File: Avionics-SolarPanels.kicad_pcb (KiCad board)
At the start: 4 copper layers, 82 x 100 mm, 208 parts, among them J1 200528-0100, J2 200528-0100, Q1 IRLML2803, Q17 NX3008NBKS, Q18 MBT2222ADW1T1, Q19 NX3008NBKS, Q2 SiRA99DP, Q20 MBT2222ADW1T1, Q21 NX3008NBKS, Q22 MBT2222ADW1T1, Q23 NX3008NBKS, Q24 MBT2222ADW1T1, Q25 NX3008NBKS, Q26 MBT2222ADW1T1, Q3 SiRA99DP, Q4 SiRA99DP, Q5 SiRA99DP, Q7 NX3008NBKS, Q8 MBT2222ADW1T1, U1 LTC4412xS6, U10 LTC3130, U11 LTC3130, U12 LTC3130, U13 ADM1176-1ARMZ-R7, U2 DRV8235RTER, U4 LTC4412xS6, U5 OPT4003DNPRQ1, U6 USBLC6-2P6, U8 LTC4412xS6

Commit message: v3.1 Updates
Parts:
- removed the C24 at (130.6, 116.6)
- removed the C25 at (130.6, 115.1)
- removed the C26 at (149.2, 89.2)
- removed the C36 at (149.9, 63.2)
- removed the F2 at (144.5, 94.2)
- removed the Q1 at (150.1, 93.5)
- removed the Q2 at (143.8, 89.2)
- removed R102, R103, R104, R105, R110, R111, R112, R113: 0R, Resistor_SMD:R_0603_1608Metric
- removed the R38 at (147.3, 93.5)
- removed the R39 at (147.6, 96.3)
- removed the R40 at (139.4, 94.5)
- removed the R41 at (137.7, 94.5)
- removed the R42 at (130.6, 113.5)
- removed the R43 at (132.3, 113.5)
- removed the R48 at (160.5, 90.4)
- removed the R50 at (162.1, 90.4)
- removed the U5 at (152.7, 63.2)
- removed the U6 at (133.6, 117.1)
- added ?: , clipboard:eb50a26b-5fb6-463a-8dd0-ee5887daaa13, F.Cu at (148.3, 55.0)
- added C1: 100n, Capacitor_SMD:C_0603_1608Metric, F.Cu at (148.2, 62.8)
- added C37: 10u, Capacitor_SMD:C_1210_3225Metric, B.Cu at (146.2, 91.0)
- added C43: 100n, Capacitor_SMD:C_0603_1608Metric, B.Cu at (129.5, 115.6)
- added F10: 500mA, Fuse:Fuse_0603_1608Metric, B.Cu at (141.5, 96.5)
- added Q16: SiRA99DP, Argus-Miscellaneous:PowerPAK SO-8, B.Cu at (140.0, 91.2)
- added Q17: IRLML2803, Package_TO_SOT_SMD:SOT-23, B.Cu at (135.1, 95.4)
- added R1: 0R, Resistor_SMD:R_0603_1608Metric, F.Cu at (149.7, 62.0)
- added R2: 0R, Resistor_SMD:R_0603_1608Metric, F.Cu at (149.7, 63.6)
- added R64: 2.7k, Resistor_SMD:R_0603_1608Metric, B.Cu at (132.7, 94.9)
- added R65: 10k, Resistor_SMD:R_0603_1608Metric, B.Cu at (131.9, 92.7)
- added R66: 4k7, Resistor_SMD:R_0603_1608Metric, B.Cu at (134.9, 92.7)
- added R67: 10k, Resistor_SMD:R_0603_1608Metric, B.Cu at (138.6, 96.5)
- added REF**: X Label, X Label, F.Cu at (152.4, 58.0)
- added Ref**: Val**, custom-footprints:ypanel, F.Cu at (169.4, 57.3)
- added U1: OPT4003DNPRQ1, Argus-IC:OPT4003, F.Cu at (152.4, 62.8)
- added U10: USBLC6-2SC6, Package_TO_SOT_SMD:SOT-23-6, B.Cu at (133.6, 114.4)
- added kibuzzard-680A9610: G***, kibuzzard-680A9610, B.Cu at (129.1, 94.8)
- C10: renamed from C7; value 1uF -> 1u
- C11: renamed from C8; value 22nF -> 22n
- C12: renamed from C9; value 22nF -> 22n
- C13: renamed from C11; value 1uF -> 1u
- C14: renamed from C12; value 47uF -> 47u
- C15: renamed from C10; value 4.7uF -> 4u7
- C16: renamed from C13; value 47uF -> 47u
- C17: renamed from C14; value 10uF -> 10u
- C18: renamed from C15; value 1uF -> 1u
- C19: renamed from C16; value 1uF -> 1u
- C2: renamed from C37; value 10nF -> 10n
- C20: renamed from C17; value 22nF -> 22n
- C21: renamed from C18; value 22nF -> 22n
- C22: renamed from C20; value 1uF -> 1u
- C23: renamed from C21; value 47uF -> 47u
- C24: renamed from C19; value 4.7uF -> 4u7
- C25: renamed from C23; value 47uF -> 47u
- C26: renamed from C39; value 10uF -> 10u
- C27: renamed from C40; value 1uF -> 1u
- C28: renamed from C41; value 1uF -> 1u
- C29: renamed from C42; value 22nF -> 22n
- C3: renamed from C38; value 10nF -> 10n
- C30: renamed from C43; value 22nF -> 22n
- C31: renamed from C45; value 1uF -> 1u
- C32: renamed from C46; value 47uF -> 47u
- C33: renamed from C44; value 4.7uF -> 4u7
- C34: renamed from C1; value 0.1uF -> 100n
- C35: renamed from C2; value 0.1uF -> 100n
- C36: renamed from C3; value 0.1uF -> 100n
- C38: renamed from C27; value 0.1uF -> 100n
- C39: renamed from C34; value 10nF -> 10n
- C4: renamed from C47; value 3.3nF -> 3n3
- C40: renamed from C35; value 10nF -> 10n
- C41: renamed from C22; value 1nF -> 1n
- C42: renamed from C28; value 0.1uF -> 100n
- C5: renamed from C48; value 10nF -> 10n
- C6: renamed from C49; value 10nF -> 10n
- C7: renamed from C4; value 47uF -> 47u
- C8: renamed from C5; value 10uF -> 10u
- C9: renamed from C6; value 1uF -> 1u
- F1: moved to B.Cu
- H1, H4: footprint MountingHole:MountingHole_3.2mm_M3_DIN965_Pad_TopBottom -> Argus-Miscellaneous:MountingHole_3.2mm_5.2mm_Slot_TopBottom
- H5, H6: footprint MountingHole:MountingHole_3mm_Pad_TopBottom -> MountingHole:MountingHole_2.2mm_M2_DIN965_Pad_TopOnly; moved to F.Cu
- J1, J2: value 200528-0100 -> 1-84952-0; footprint Argus-Connectors:Molex_200528-0100_1x10-1MP_P1.00mm_Horizontal -> Connector_FFC-FPC:TE_1-84952-0_1x10-1MP_P1.0mm_Horizontal
- L1, L2, L3: value 6.8uH -> 6.8u
- R10: renamed from R122; value 10K -> 10k
- R12: renamed from R119; value 100K -> 100k
- R13: renamed from R123; value 200K -> 200k
- R14: renamed from R120; value DNI (0R) -> 0R
- R19: renamed from R25; value 100K -> 100k
- R21: renamed from R35; value 200K -> 200k
- R26: value 100K -> 100k
- R28: renamed from R89; value 200K -> 200k
- R3: renamed from R115; value 10K -> 10k
- R33: renamed from R27; value 100K -> 100k
- R35: renamed from R109; value 200K -> 200k
- R36: value 2.7k -> 0R
- R37: value 10k -> 0R
- R38: renamed from R124; value ?R -> 0.01R
- R39: renamed from R125; value 1K -> 1k
- R4: renamed from R116; value 10K -> 10k
- R40: renamed from R129; value 10K -> 10k
- R41: renamed from R130; value 10K -> 10k
- R43: renamed from R127; value 100K -> 100k
- R44: renamed from R131; value 200K -> 200k
- R45: renamed from R128; value DNI (0R) -> 0R
- R46: renamed from R135; value 10K -> 10k
- R47: renamed from R136; value 10K -> 10k
- R49: renamed from R133; value 100K -> 100k
- R50: renamed from R137; value 200K -> 200k
- R51: renamed from R134; value DNI (0R) -> 0R
- R52: renamed from R1; value 0R (DNI) -> 0R
- R56: renamed from R5; value 0R (DNI) -> 0R
- R6: renamed from R107; value 100K -> 100k
- R60: renamed from R9; value 0R (DNI) -> 0R
- R7: renamed from R117; value 200K -> 200k
- R70: renamed from R86; value 10K -> 10k
- R71: renamed from R87; value 10K -> 10k
- R73: renamed from R85; value 100K -> 100k
- R74: renamed from R94; value 200K -> 200k
- R75: renamed from R95; value DNI (0R) -> 0R
- R76: renamed from R99; value 10K -> 10k
- R77: renamed from R100; value 10K -> 10k
- R79: renamed from R97; value 100K -> 100k
- R8: renamed from R114; value DNI (0R) -> 0R
- R80: renamed from R101; value 200K -> 200k
- R81: renamed from R98; value DNI (0R) -> 0R
- R9: renamed from R121; value 10K -> 10k
- SC1, SC2, SC4, SC5, SC6: value SM141K06L -> SM141K06TF
- moved F1 35.3 mm to (173.6, 84.8)
- moved C6 24.1 mm to (136.8, 73.1), turned to 90 degrees
- moved R40 23.8 mm to (131.1, 72.3), turned to 0 degrees
- moved R50 23.1 mm to (135.3, 73.1), turned to -90 degrees
- moved R49 22.4 mm to (133.6, 73.1), turned to -90 degrees
- moved R37 22.2 mm to (133.1, 109.9)
- moved R42 20.8 mm to (131.1, 73.8), turned to 0 degrees
- moved R36 20.2 mm to (129.7, 109.9), turned to 0 degrees
- moved Q8 18.1 mm to (135.9, 75.8), turned to 0 degrees
- moved Q5 16.5 mm to (131.3, 75.8), turned to 0 degrees
- moved R47 16.4 mm to (133.6, 76.0), turned to 90 degrees
- moved R51 14.4 mm to (135.9, 77.8), turned to 0 degrees
- moved R45 12.3 mm to (131.3, 77.8), turned to 180 degrees
- moved R9 12.2 mm to (168.7, 72.3), turned to 0 degrees
- moved C39 11.9 mm to (168.0, 99.4), turned to -90 degrees
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- renumbered F6 to F2, F7 to F3, F8 to F4, F9 to F5, F10 to F6, F3 to F7, F4 to F8, F5 to F9, Q20 to Q1, Q4 to Q10, Q5 to Q11, Q8 to Q12, Q7 to Q13, Q18 to Q14, Q17 to Q15, Q19 to Q2, Q22 to Q3, Q21 to Q4, Q24 to Q5, Q23 to Q6, Q26 to Q7, Q25 to Q8, Q3 to Q9, R118 to R11, R16 to R15, R17 to R16, R13 to R17, R22 to R18, R34 to R20, R18 to R22, R19 to R23, R14 to R24, R23 to R25, R88 to R27, R20 to R29, R21 to R30, R15 to R31, R24 to R32, R108 to R34, R126 to R42, R132 to R48, R106 to R5, R2 to R53, R3 to R54, R4 to R55, R6 to R57, R7 to R58, R8 to R59, R10 to R61, R11 to R62, R12 to R63, R33 to R68, R54 to R69, R60 to R72, R96 to R78, R28 to R82, R29 to R83, R30 to R84, R31 to R85, R49 to R86, R51 to R87, R32 to R88, R52 to R89, R53 to R90, U13 to U2, U1 to U3, U8 to U5, U10 to U6, U11 to U7, U12 to U8, U2 to U9
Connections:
- net /Coil Driver/A0_COIL renamed /Coil Driver/A0
- net /Coil Driver/A1_COIL renamed /Coil Driver/A1
- net /Solar Charger/I2C Single Protection4/DEVICE renamed /Solar Charger/I2C Single Protection2/DEVICE
- net /Solar Charger/I2C Single Protection5/DEVICE renamed /Solar Charger/I2C Single Protection3/DEVICE
- net /Solar Charger/MPPT1/VIN renamed /Solar Charger/DSOLAR1
- net /Solar Charger/MPPT2/VIN renamed /Solar Charger/DSOLAR2
- F1 pad 2: PERI_3V3 -> 3V3_P
- J2 pad 1: Net-(J2-Pin_1) -> /Interfaces/SCL_C
- J2 pad 2: Net-(J2-Pin_2) -> /Interfaces/SDA_C
- J2 pad 3: /Interfaces/COIL_DRIVER_EN_OR_MAIN_3V3 -> COIL_DRIVER_EN
- J2 pad 4: MAIN_3V3 -> 3V3_P
- J2 pad 5: /Interfaces/PERI_3V3_OR_GND -> 3V3_P
- R36 pad 1: COIL_DRIVER_EN -> GND
- R36 pad 2: Net-(D9-A) -> /Solar Charger/A0
- R37 pad 2: COIL_DRIVER_EN -> /Solar Charger/A1
- R40 pad 1: MAIN_3V3 -> 3V3_P
- R41 pad 1: MAIN_3V3 -> 3V3_P
- R43 pad 1: MAIN_3V3 -> 3V3_P
- R46 pad 1: MAIN_3V3 -> 3V3_P
- R47 pad 1: MAIN_3V3 -> 3V3_P
- R49 pad 1: MAIN_3V3 -> 3V3_P
- R68 pad 1: MAIN_3V3 -> 3V3_P
- R69 pad 2: PERI_3V3 -> 3V3_P
- R70 pad 1: MAIN_3V3 -> 3V3_P
- R71 pad 1: MAIN_3V3 -> 3V3_P
- R73 pad 1: MAIN_3V3 -> 3V3_P
- R76 pad 1: MAIN_3V3 -> 3V3_P
- R77 pad 1: MAIN_3V3 -> 3V3_P
- R79 pad 1: MAIN_3V3 -> 3V3_P
- R89 pad 1: MAIN_3V3 -> 3V3_P
- U2 pad 8: /Solar Charger/A0_S -> /Solar Charger/A0
- U2 pad 9: /Solar Charger/A1_S -> /Solar Charger/A1
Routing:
- net /Coil Driver/coil: track 18961.3 -> 14514.8 mm
- net PERI_3V3: track 101.5 -> 0.00 mm, vias 3 -> 0
- net GND: track 93.6 -> 0.00 mm, vias 172 -> 66
- net VBATT: track 57.2 -> 2.96 mm, vias 2 -> 6
- net MAIN_3V3: track 41.3 -> 0.00 mm, vias 12 -> 0
- net SCL: track 93.4 -> 131.4 mm, vias 3 -> 4
- net /Interfaces/COIL_DRIVER_EN_OR_MAIN_3V3: track 35.6 -> 0.00 mm, vias 2 -> 0
- net Net-(D1-K): track 54.4 -> 82.8 mm
- net /Light Sensor/LS_3V3: track 65.2 -> 37.3 mm, vias 4 -> 6
- net Net-(D4-K): track 55.2 -> 82.8 mm
- net Net-(D3-K): track 147.2 -> 174.5 mm
- net 3V3_P: track 0.00 -> 17.8 mm, vias 0 -> 16
- net /Light Sensor/ADDR_LS: track 17.4 -> 0.00 mm
- net /Solar Charger/I2C Single Protection3/DEVICE: track 26.0 -> 42.3 mm
- net COIL_DRIVER_EN: track 13.2 -> 27.5 mm, vias 0 -> 2
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- added copper zone on In2.Cu, net /Light Sensor/LS_3V3
- added copper zone on B.Cu, net 3V3_P
- added copper zone on In2.Cu, net 3V3_P
- added copper zone on B.Cu, net D_VSOLAR1
- added copper zone on B.Cu, net D_VSOLAR2
- added copper zone on B.Cu, net Net-(Q16-S)
- added copper zone on In2.Cu, net VBATT
- removed copper zone on In2.Cu, net MAIN_3V3
- removed copper zone on B.Cu, net Net-(Q2-S)
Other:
- outline, holes or cut-outs redrawn
- board text added: "ARGUS CUBESAT"
- board text added: "ARGUS Cubesat Carnegie Mellon University X/Y Solar Panel v3.1"
- board text added: "COIL DRIVER I2C BUS PROTECTION"
- board text added: "CURRENT SENSOR I2C BUS PROTECTION"
- board text added: "LIGHT SENSOR I2C BUS PROTECTION"
- board text added: "N"
- board text added: "P"
- board text added: "SENSE"
- board text added: "⊗"
- board text added: "⊙"
- board text removed: "ARGUS"
- board text removed: "ARGUS Cubesat Carnegie Mellon University X/Y Solar Panel v3"

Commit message: Local Stash
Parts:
- removed U10: USBLC6-2SC6, Package_TO_SOT_SMD:SOT-23-6
- added U11: D5V0P4UR6SO, Package_TO_SOT_SMD:SOT-23-6, B.Cu at (133.6, 114.4)
- R64: value 2.7k -> 2k7
- SC1, SC2, SC4, SC5, SC6: value SM141K06TF -> SM141K06TF/S; footprint Argus-Miscellaneous:SM141K06TF -> Argus-Miscellaneous:SM141K06TF_S
- SC3: value SM141K10TF -> SM141K10TF/S; footprint Argus-Miscellaneous:SM141K10TF -> Argus-Miscellaneous:SM141K10TF_S
- moved D1 0.51 mm to (114.6, 81.5)
- moved D4 0.51 mm to (190.2, 81.5)
- moved SC1 0.51 mm to (128.4, 81.5)
- moved SC4 0.51 mm to (176.4, 81.5)
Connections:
- J2 pad 1: /Interfaces/SCL_C -> SCL
- J2 pad 2: /Interfaces/SDA_C -> SDA
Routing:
- net Net-(D4-K): track 82.8 -> 75.5 mm
- net Net-(D1-K): track 82.8 -> 75.5 mm
- net SCL: track 131.4 -> 135.9 mm
- net SDA: track 135.1 -> 139.5 mm
- net Net-(D2-K): track 84.8 -> 81.8 mm
- net /Interfaces/SCL_C: track 2.95 -> 0.00 mm
- net /Interfaces/SDA_C: track 2.94 -> 0.00 mm
- net Net-(Q9-G): track 6.69 -> 6.03 mm
- net Net-(Q11-G): track 6.75 -> 6.10 mm
- net Net-(Q10-G): track 6.73 -> 6.15 mm
- net VBATT: track 2.96 -> 2.40 mm
- net /Solar Charger/VCHRG: track 2.96 -> 2.40 mm
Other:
- board text added: "3V3_P"
- board text removed: "M_3V3"
- board text removed: "P_3V3"

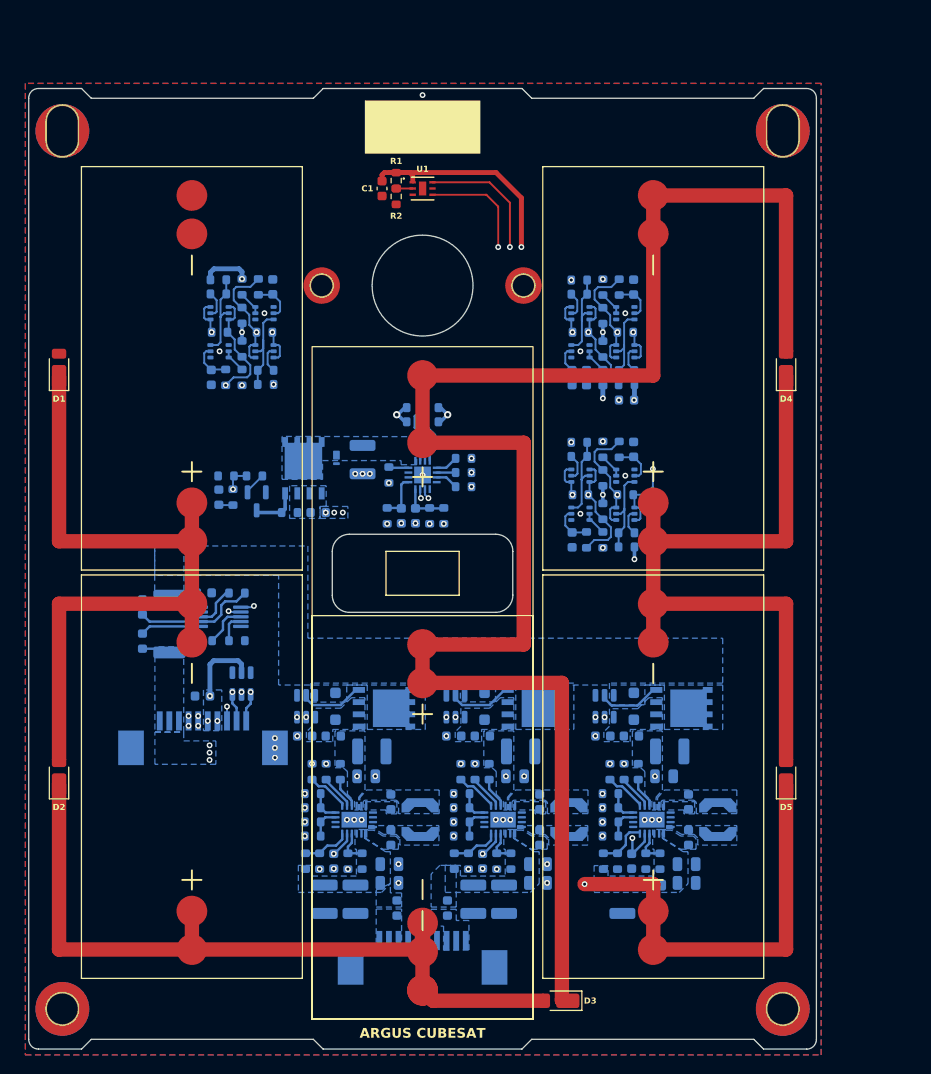
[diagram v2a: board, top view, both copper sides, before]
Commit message: Updated access port, added deployment sensor
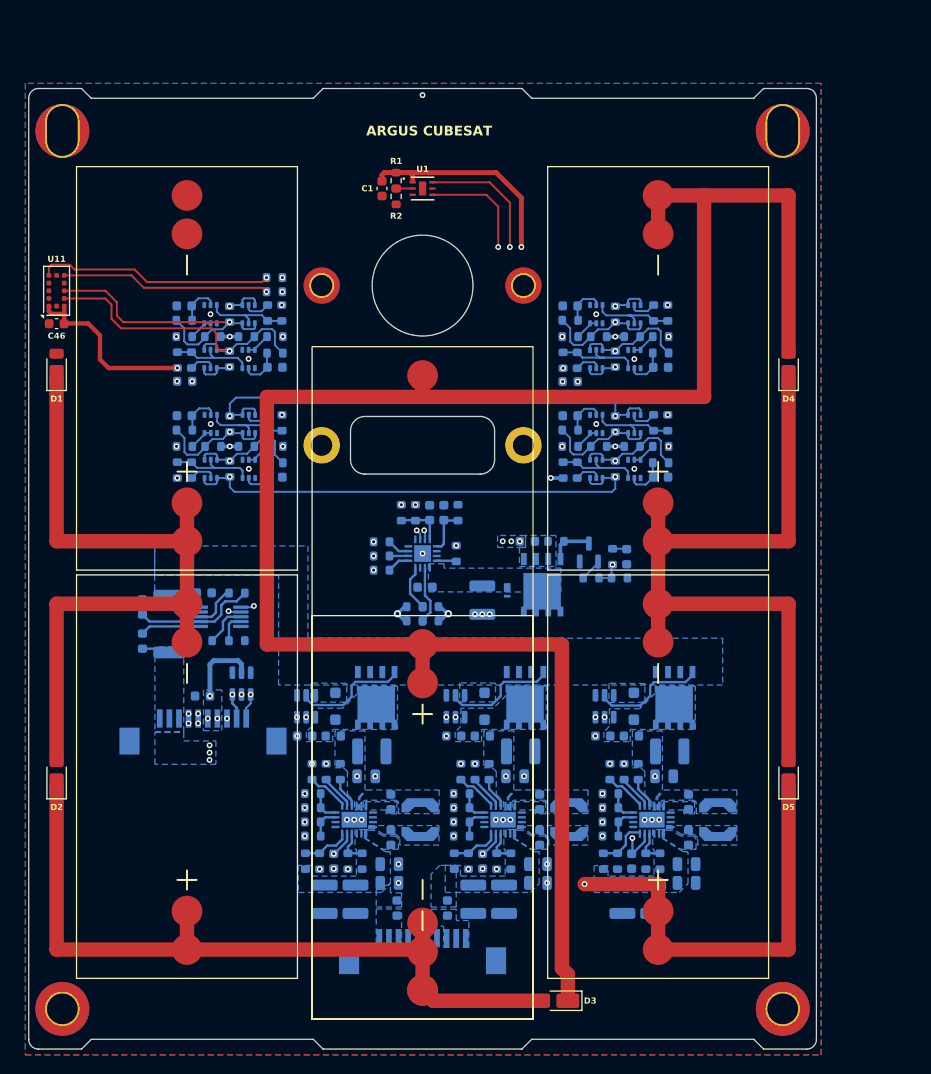
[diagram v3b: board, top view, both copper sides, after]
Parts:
- removed ?: , clipboard:eb50a26b-5fb6-463a-8dd0-ee5887daaa13
- removed the Q10 at (164.6, 116.9)
- removed the Q11 at (149.1, 116.9)
- removed the Q9 at (180.1, 116.9)
- removed REF**: X Label, X Label
- removed Ref**: Val**, custom-footprints:ypanel
- added C44: 10n, Capacitor_SMD:C_0603_1608Metric, B.Cu at (127.6, 75.0)
- added C45: 10n, Capacitor_SMD:C_0603_1608Metric, B.Cu at (137.0, 81.4)
- added C46: 100n, Capacitor_SMD:C_0603_1608Metric, F.Cu at (114.3, 76.9)
- added F11: 250mA, Fuse:Fuse_0603_1608Metric, B.Cu at (127.6, 82.9)
- added H7: Access Port, Argus-Miscellaneous:Access Port 2, F.Cu at (152.4, 89.5)
- added Q14: SIRA99DP-T1-GE3, Package_SO:PowerPAK_SO-8_Single, B.Cu at (164.8, 104.1)
- added Q15: SIRA99DP-T1-GE3, Package_SO:PowerPAK_SO-8_Single, B.Cu at (178.6, 115.8)
- added Q17: SIRA99DP-T1-GE3, Package_SO:PowerPAK_SO-8_Single, B.Cu at (147.6, 115.8)
- added Q18: MBT2222ADW1T1, Package_TO_SOT_SMD:SOT-363_SC-70-6, B.Cu at (134.3, 75.9)
- added Q19: NX3008NBKS, Package_TO_SOT_SMD:SOT-363_SC-70-6, B.Cu at (130.3, 75.9)
- added Q20: MBT2222ADW1T1, Package_TO_SOT_SMD:SOT-363_SC-70-6, B.Cu at (130.3, 80.6)
- added Q21: NX3008NBKS, Package_TO_SOT_SMD:SOT-363_SC-70-6, B.Cu at (134.3, 80.6)
- added R100: 10k, Resistor_SMD:R_0603_1608Metric, B.Cu at (130.6, 78.2)
- added R101: 200k, Resistor_SMD:R_0603_1608Metric, B.Cu at (127.6, 76.5)
- added R102: 200k, Resistor_SMD:R_0603_1608Metric, B.Cu at (137.0, 79.9)
- added R103: 10k, Resistor_SMD:R_0603_1608Metric, B.Cu at (137.0, 73.6)
- added R104: 10k, Resistor_SMD:R_0603_1608Metric, B.Cu at (137.0, 72.1)
- added R91: 680R, Resistor_SMD:R_0603_1608Metric, B.Cu at (128.3, 80.7)
- added R92: 680R, Resistor_SMD:R_0603_1608Metric, B.Cu at (136.3, 75.8)
- added R93: 100k, Resistor_SMD:R_0603_1608Metric, B.Cu at (137.0, 78.2)
- added R94: 100k, Resistor_SMD:R_0603_1608Metric, B.Cu at (127.6, 78.2)
- added R95: 0R, Resistor_SMD:R_0603_1608Metric, B.Cu at (132.3, 80.6)
- added R96: 0R, Resistor_SMD:R_0603_1608Metric, B.Cu at (132.3, 75.9)
- added R97: 10k, Resistor_SMD:R_0603_1608Metric, B.Cu at (126.9, 80.7)
- added R98: 10k, Resistor_SMD:R_0603_1608Metric, B.Cu at (137.7, 75.8)
- added R99: 10k, Resistor_SMD:R_0603_1608Metric, B.Cu at (134.1, 78.2)
- added U11: VL53L4CX, Sensor_Distance:ST_VL53L1x, F.Cu at (114.3, 73.5)
- D10: value 10V -> PTVS10VZ1USK
- F2, F3, F4: value 100mA -> 500mA
- J1, J2: value 1-84952-0 -> 522711069; footprint Connector_FFC-FPC:TE_1-84952-0_1x10-1MP_P1.0mm_Horizontal -> Argus-Connectors:CON_522711069_MOL
- Q16: value SiRA99DP -> SIRA99DP-T1-GE3; footprint Argus-Miscellaneous:PowerPAK SO-8 -> Package_SO:PowerPAK_SO-8_Single
- R36, R37: value 0R -> ?R
- R38: value 0.01R -> 10m
- U6, U7, U8: value LTC3130 -> LTC3130IUDC
- moved kibuzzard-680A9610 47.0 mm to (175.7, 101.3), turned to -90 degrees
- moved D9 42.9 mm to (173.7, 101.1), turned to 90 degrees
- moved R65 42.3 mm to (172.9, 103.4), turned to 180 degrees
- moved R64 40.0 mm to (172.2, 101.1), turned to 90 degrees
- moved R66 36.6 mm to (169.9, 103.4), turned to 180 degrees
- moved Q13 35.0 mm to (169.7, 100.7), turned to 90 degrees
- moved Q16 33.8 mm to (163.1, 115.8)
- moved R67 27.9 mm to (166.3, 99.5), turned to 180 degrees
- moved D10 22.5 mm to (161.2, 104.6)
- moved R82 22.3 mm to (153.2, 107.8), turned to 0 degrees
- moved R83 22.3 mm to (151.6, 107.8), turned to 0 degrees
- moved F10 22.0 mm to (163.3, 99.5), turned to 180 degrees
- moved R40 20.3 mm to (126.9, 92.1), turned to 90 degrees
- moved R85 19.3 mm to (153.2, 106.3), turned to 180 degrees
- moved R84 19.3 mm to (151.6, 106.3), turned to 180 degrees
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- renumbered Q13 to Q10, Q14 to Q11, Q15 to Q12, Q17 to Q13, Q12 to Q9, U11 to U10
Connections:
- F10 pad 1: Net-(Q16-S) -> Net-(F10-Pad1)
- Q13 pad 3: Net-(Q16-G) -> Net-(Q13-D)
- Q16 pad 1: Net-(Q16-G) -> /Solar Charger/VCHRG
- Q16 pad 2: /Coil Driver/VM -> /Solar Charger/VCHRG
- Q16 pad 3: Net-(Q16-S) -> /Solar Charger/VCHRG
- R67 pad 1: Net-(Q16-G) -> Net-(Q13-D)
- R67 pad 2: Net-(Q16-S) -> Net-(F10-Pad1)
- U4 pad 5: Net-(Q10-G) -> Net-(Q16-G)
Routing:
- net SCL: track 135.9 -> 102.2 mm, vias 4 -> 5
- net /Deployment Sensor/SCL_DS: track 0.00 -> 33.2 mm, vias 0 -> 1
- net /Deployment Sensor/SDA_DS: track 0.00 -> 31.5 mm, vias 0 -> 1
- net COIL_DRIVER_EN: track 27.4 -> 56.8 mm
- net Net-(D3-K): track 174.1 -> 200.1 mm
- net Net-(U11-XSHUT): track 0.00 -> 24.6 mm, vias 0 -> 1
- net Net-(U11-GPIO1): track 0.00 -> 21.8 mm, vias 0 -> 1
- net /Coil Driver/coil: track 14514.4 -> 14493.1 mm
- net /Deployment Sensor/DS_3V3: track 0.00 -> 21.1 mm, vias 0 -> 8
- net SDA: track 139.5 -> 126.5 mm, vias 4 -> 5
- net /Solar Charger/I2C Single Protection3/DEVICE: track 42.0 -> 32.5 mm
- net Net-(Q18B-B2): track 0.00 -> 8.93 mm
- net Net-(Q20B-B2): track 0.00 -> 8.77 mm
- net /Coil Driver/SCL_M: track 32.8 -> 41.4 mm
- net Net-(Q16-G): track 4.75 -> 11.8 mm
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- added copper zone on In2.Cu, net /Deployment Sensor/DS_3V3
- added copper zone on B.Cu, net Net-(F10-Pad1)
- removed copper zone on B.Cu, net Net-(Q16-S)
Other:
- outline, holes or cut-outs redrawn
- board text added: "DEPLOYMENT SENSOR I2C BUS PROTECTION"
- board text added: "TO MAINBOARD"
- board text removed: "MAINBOARD"

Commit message: Local Stash
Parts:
- added R118: 0R, Resistor_SMD:R_0603_1608Metric, F.Cu at (201.1, 129.4)
- added R119: 0R, Resistor_SMD:R_0603_1608Metric, F.Cu at (201.1, 131.9)
- added R120: 0R, Resistor_SMD:R_0603_1608Metric, F.Cu at (201.1, 134.4)
- R1, R2, R86, R87: value 0R -> ?R
- R15: value 1.91M -> 1.8M
- R16: value 126k -> 100k
- R17: value 1.91M -> 2.10M
- R18: value 182k -> 137k
- R20, R27, R34: value 1.47M -> 2M
- R21, R28, R35: value 200k -> 270k
- R22, R29: value 1.91M -> 2M
- R23, R30: value 126k -> 127k
- R24, R31: value 1.91M -> 1.87M
- R25, R32: value 182k -> 140k
- R88: value TBD -> 560R
- R89: value TBD -> 2k7
- R90: value TBD -> 1M
- U11: value VL53L4CX -> VL53L4CD
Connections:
- net /Solar Charger/MPPT/MPPC renamed /Solar Charger/MPPC
- net /Solar Charger/MPPT1/MPPC renamed /Solar Charger/MPPC1
- net /Solar Charger/MPPT2/MPPC renamed /Solar Charger/MPPC2
